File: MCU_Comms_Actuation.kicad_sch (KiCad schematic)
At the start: 4 parts

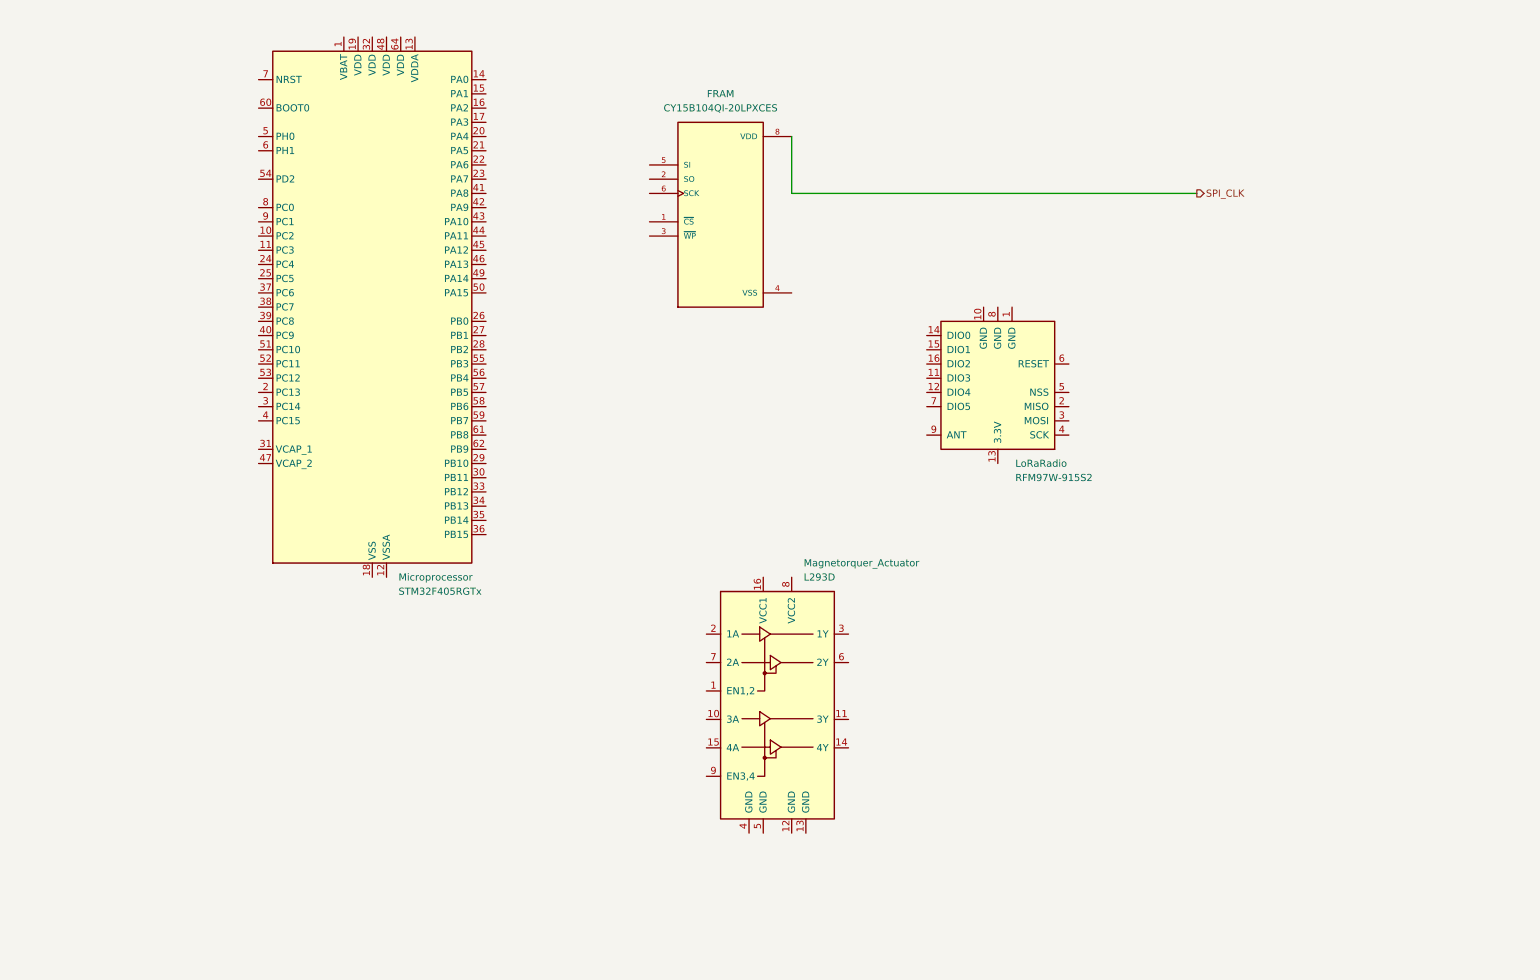
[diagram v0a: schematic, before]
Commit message: Added decoupling caps to STM32
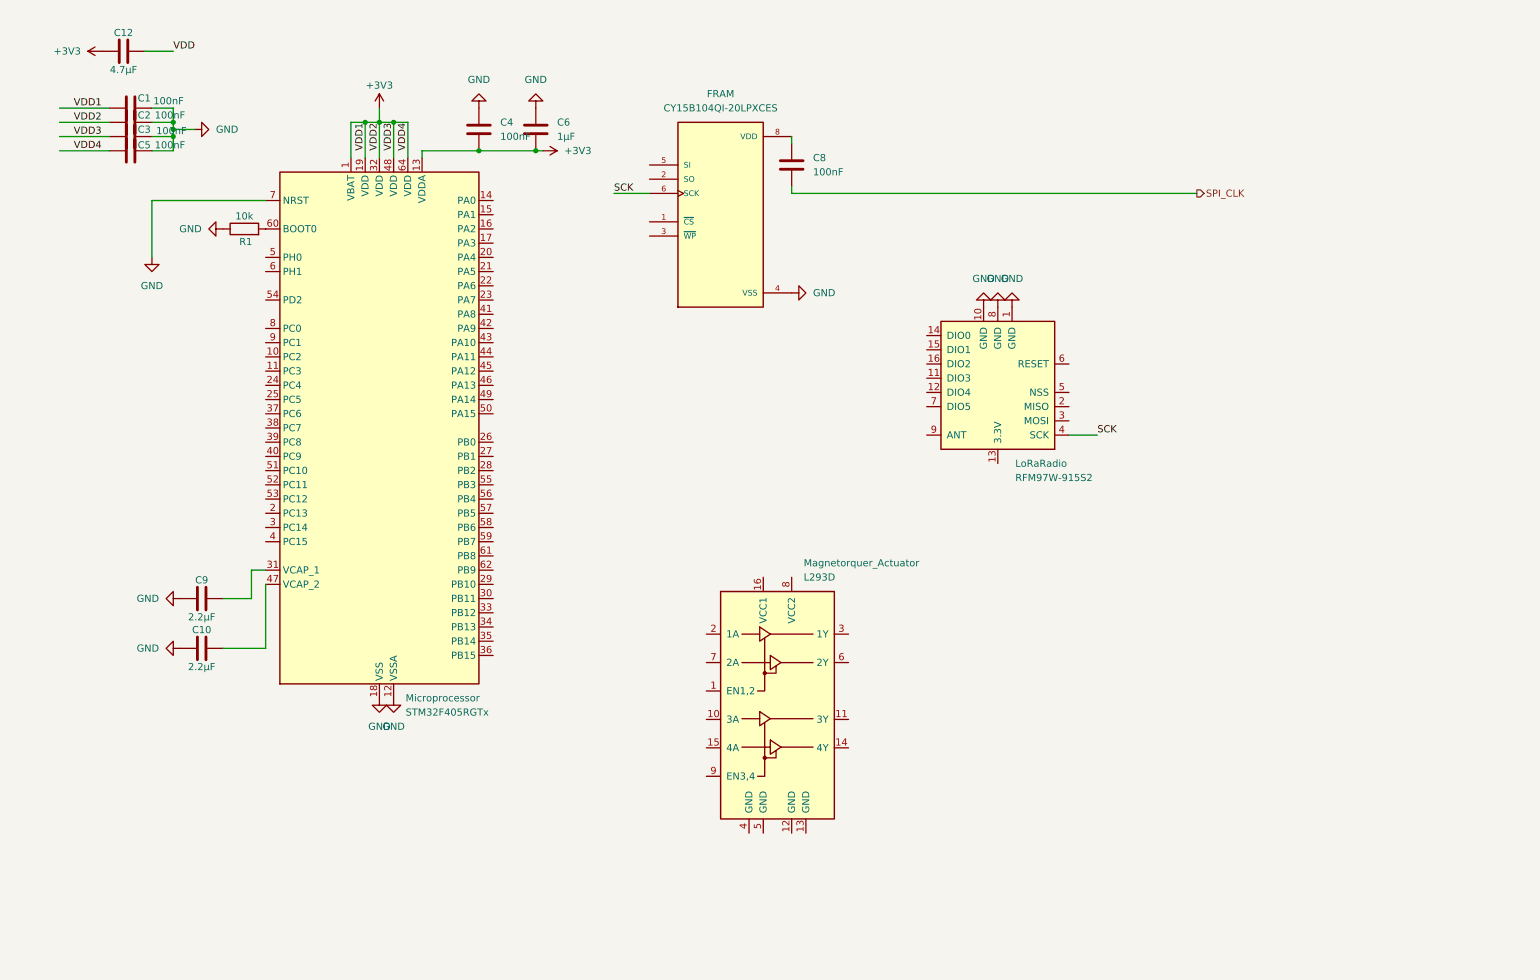
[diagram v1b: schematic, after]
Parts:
- added C1, C2, C3, C4, C5, C8: 100nF, symbol Device:C
- added C10, C9: 2.2µF, symbol Device:C
- added C12: 4.7µF, symbol Device:C
- added C6: 1µF, symbol Device:C
- added R1: 10k, symbol Device:R
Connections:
- net SPI_CLK: now also C8.2; no longer FRAM.8 (VDD)
- net GND: now reaches FRAM.4 (VSS)
- net GND: now also LoRaRadio.1 (GND), LoRaRadio.10 (GND), LoRaRadio.8 (GND), Microprocessor.12 (VSSA), Microprocessor.18 (VSS), Microprocessor.63 (VSS), Microprocessor.7 (NRST), C1.1, C10.1, C2.1, C3.1, C4.1, C5.1, C6.1, C9.1, R1.1
- net SCK: now reaches FRAM.6 (SCK)
- net SCK: now also LoRaRadio.4 (SCK)
- net +3V3: now reaches Microprocessor.1 (VBAT)
- net +3V3: now also Microprocessor.13 (VDDA), Microprocessor.19 (VDD), Microprocessor.32 (VDD), Microprocessor.48 (VDD), Microprocessor.64 (VDD), C1.2, C12.1, C2.2, C3.2, C4.2, C5.2, C6.2
- net at Microprocessor.31 (VCAP_1): now also C9.2
- net at Microprocessor.47 (VCAP_2): now also C10.2
- net at Microprocessor.60 (BOOT0): now also R1.2
- new net: C8.1, FRAM.8 (VDD)
- new net VDD: C12.2
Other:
- moved on the sheet: Microprocessor

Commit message: Add STM32 and FRAM basic pinout with decoupling caps
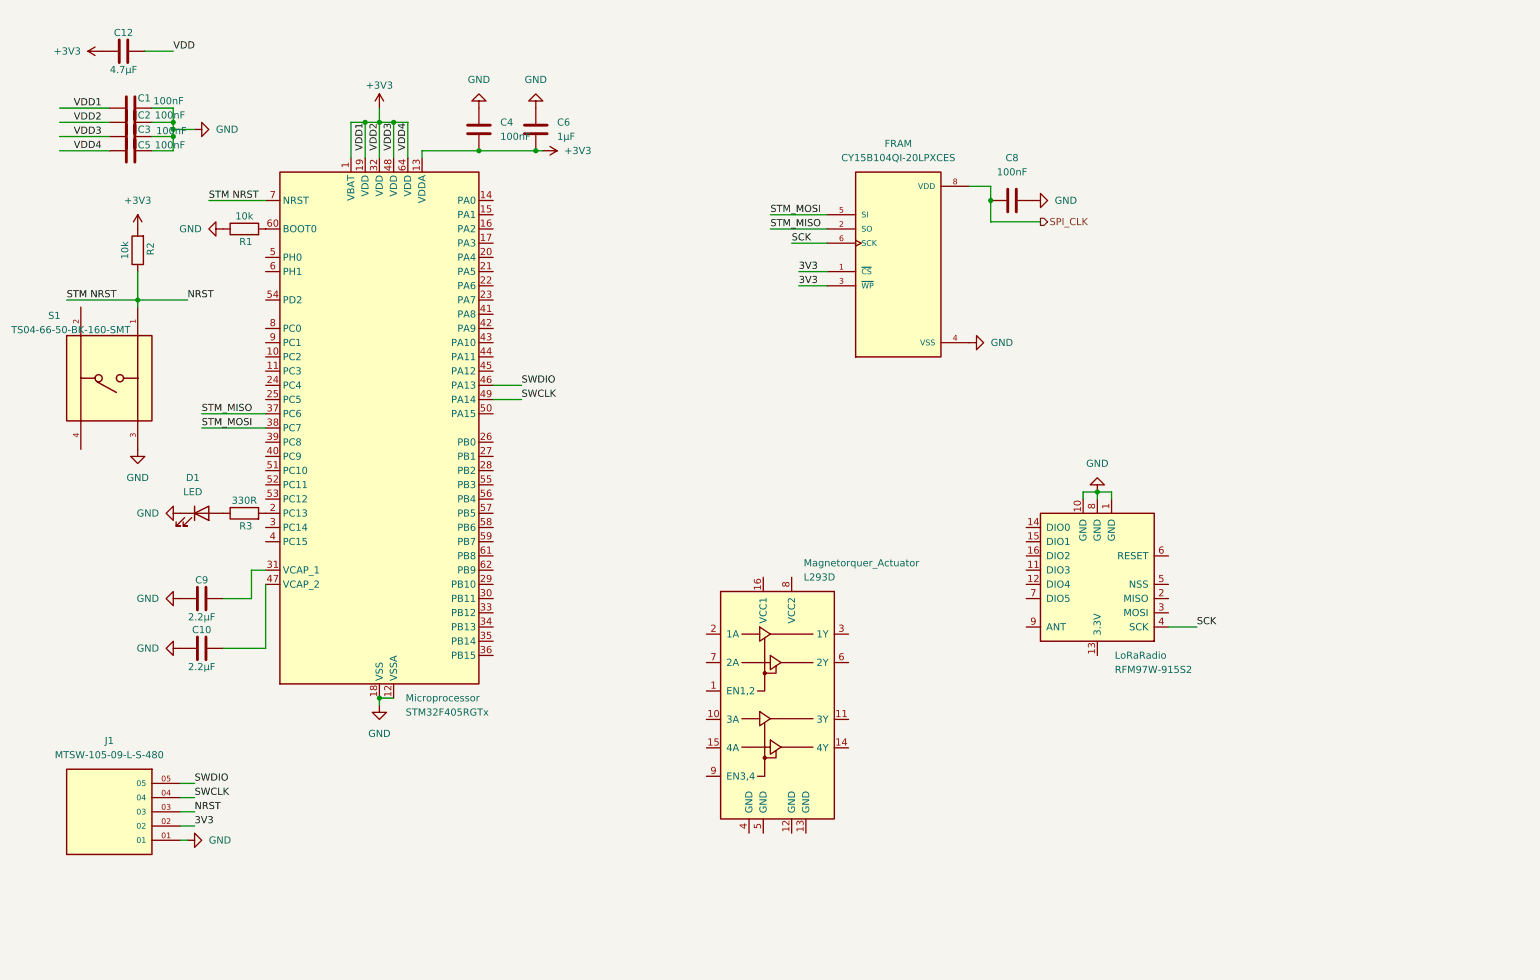
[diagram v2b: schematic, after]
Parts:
- added D1: LED, symbol Device:LED
- added J1: MTSW-105-09-L-S-480, MTSW-105-09-L-S-480:SAMTEC_MTSW-105-09-L-S-480, symbol MTSW-105-09-L-S-480:MTSW-105-09-L-S-480
- added R2: 10k, symbol Device:R
- added R3: 330R, symbol Device:R
- added S1: TS04-66-50-BK-160-SMT, TS04-66-50-BK-160-SMT:SW_TS04-66-50-BK-160-SMT, symbol TS04-66-50-BK-160-SMT:TS04-66-50-BK-160-SMT
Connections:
- net +3V3: now also R2.2
- net GND: now also C8.2, D1.1 (K), J1.01, S1.3; no longer Microprocessor.7 (NRST)
- net SPI_CLK: now also C8.1, FRAM.8 (VDD); no longer C8.2
- net 3V3: now reaches FRAM.1 (~{CS})
- net 3V3: now also FRAM.3 (~{WP}), J1.02
- net STM_MISO: now reaches FRAM.2 (SO)
- net STM_MISO: now also Microprocessor.37 (PC6)
- net STM_MOSI: now reaches FRAM.5 (SI)
- net STM_MOSI: now also Microprocessor.38 (PC7)
- net at Microprocessor.2 (PC13): now also R3.2
- net SWDIO: now reaches Microprocessor.46 (PA13)
- net SWDIO: now also J1.05
- net SWCLK: now reaches Microprocessor.49 (PA14)
- net SWCLK: now also J1.04
- new net: D1.2 (A), R3.1
- new net NRST: J1.03, Microprocessor.7 (NRST), R2.1, S1.1
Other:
- moved on the sheet: FRAM, LoRaRadio

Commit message: Fix MCU/FRAM pins, add LoRa connections
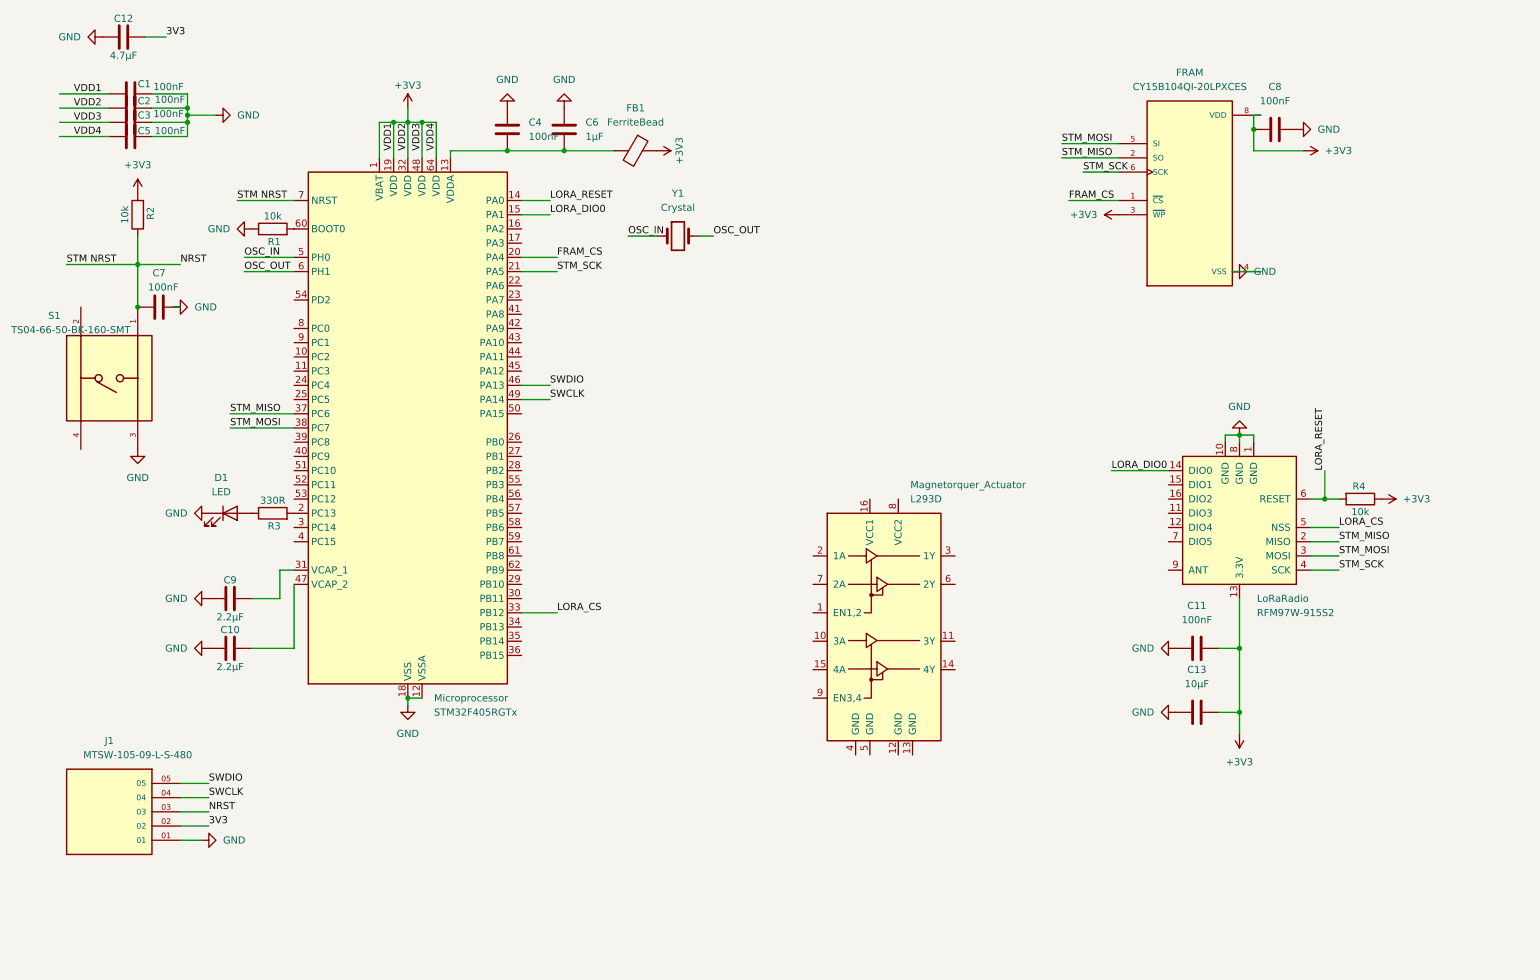
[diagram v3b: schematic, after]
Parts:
- added C11, C7: 100nF, symbol Device:C
- added C13: 10µF, symbol Device:C
- added FB1: FerriteBead, symbol Device:FerriteBead
- added R4: 10k, symbol Device:R
- added Y1: Crystal, symbol Device:Crystal
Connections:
- net SCK is gone; now on net STM_SCK: FRAM.6 (SCK), LoRaRadio.4 (SCK)
- net SPI_CLK is gone; now on net +3V3: C8.1, FRAM.8 (VDD)
- net VDD is gone; now on net 3V3: C12.2
- net +3V3: now also FRAM.3 (~{WP}), LoRaRadio.13 (3.3V), C11.2, C13.2, FB1.1, R4.1; no longer C12.1, C4.2, C6.2, Microprocessor.13 (VDDA)
- net 3V3: no longer FRAM.1 (~{CS}), FRAM.3 (~{WP})
- net GND: now also C12.1, C11.1, C13.1, C7.1
- net NRST: now also C7.2
- net STM_MISO: now also LoRaRadio.2 (MISO)
- net STM_MOSI: now also LoRaRadio.3 (MOSI)
- net LORA_RESET: now reaches Microprocessor.14 (PA0)
- net LORA_RESET: now also LoRaRadio.6 (RESET), R4.2
- net LORA_DIO0: now reaches Microprocessor.15 (PA1)
- net LORA_DIO0: now also LoRaRadio.14 (DIO0)
- net FRAM_CS: now reaches Microprocessor.20 (PA4)
- net FRAM_CS: now also FRAM.1 (~{CS})
- net STM_SCK: now reaches Microprocessor.21 (PA5)
- net LORA_CS: now reaches Microprocessor.33 (PB12)
- net LORA_CS: now also LoRaRadio.5 (NSS)
- net OSC_IN: now reaches Microprocessor.5 (PH0)
- net OSC_IN: now also Y1.1
- net OSC_OUT: now reaches Microprocessor.6 (PH1)
- net OSC_OUT: now also Y1.2
- new net: C4.2, C6.2, FB1.2, Microprocessor.13 (VDDA)
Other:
- moved on the sheet: C1, C10, C12, C2, C3, C4, C5, C6, C8, C9, D1, FRAM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

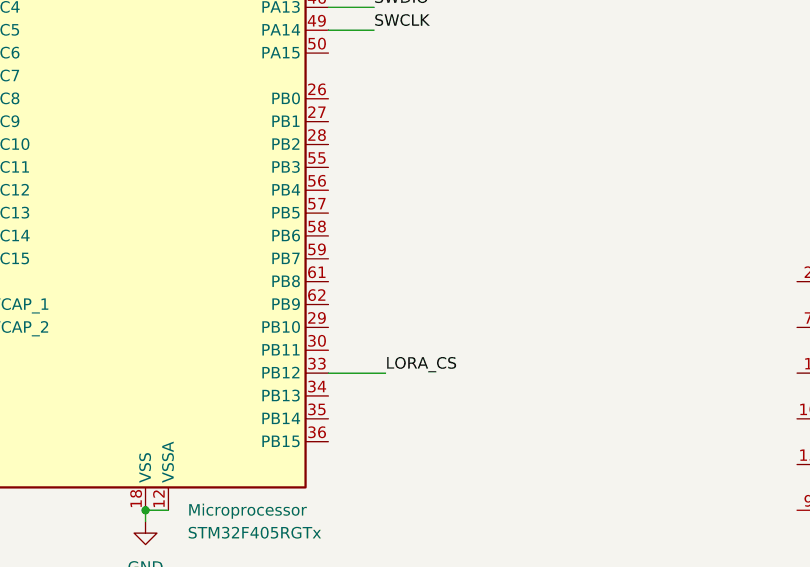
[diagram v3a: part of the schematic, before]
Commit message: Updated sensors wiring (connected pins to +3V3 and GND), added pullups and decouplers. Double check my wiring as these could be wrong.
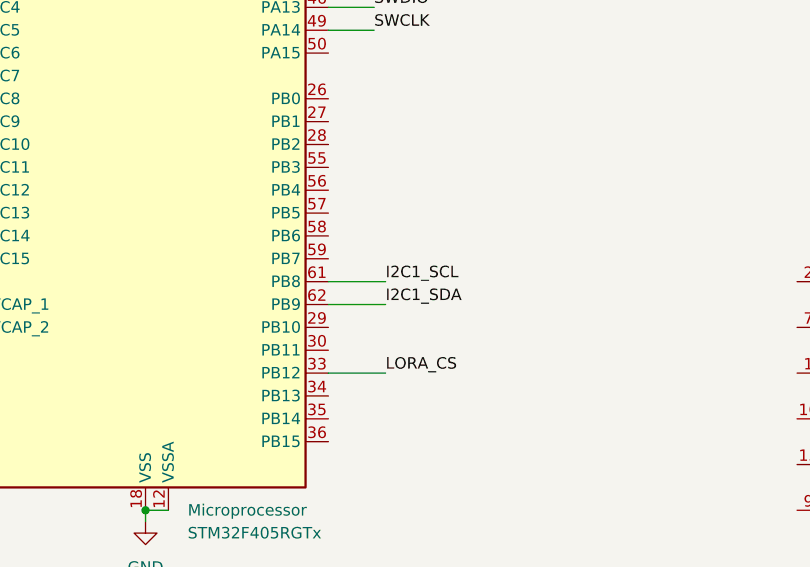
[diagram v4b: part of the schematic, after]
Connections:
- net I2C1_SCL: now reaches Microprocessor.61 (PB8)
- net I2C1_SDA: now reaches Microprocessor.62 (PB9)
